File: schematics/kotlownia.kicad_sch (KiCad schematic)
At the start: 5 parts, among them U1 MAX485E, U2 MAX31865xAP

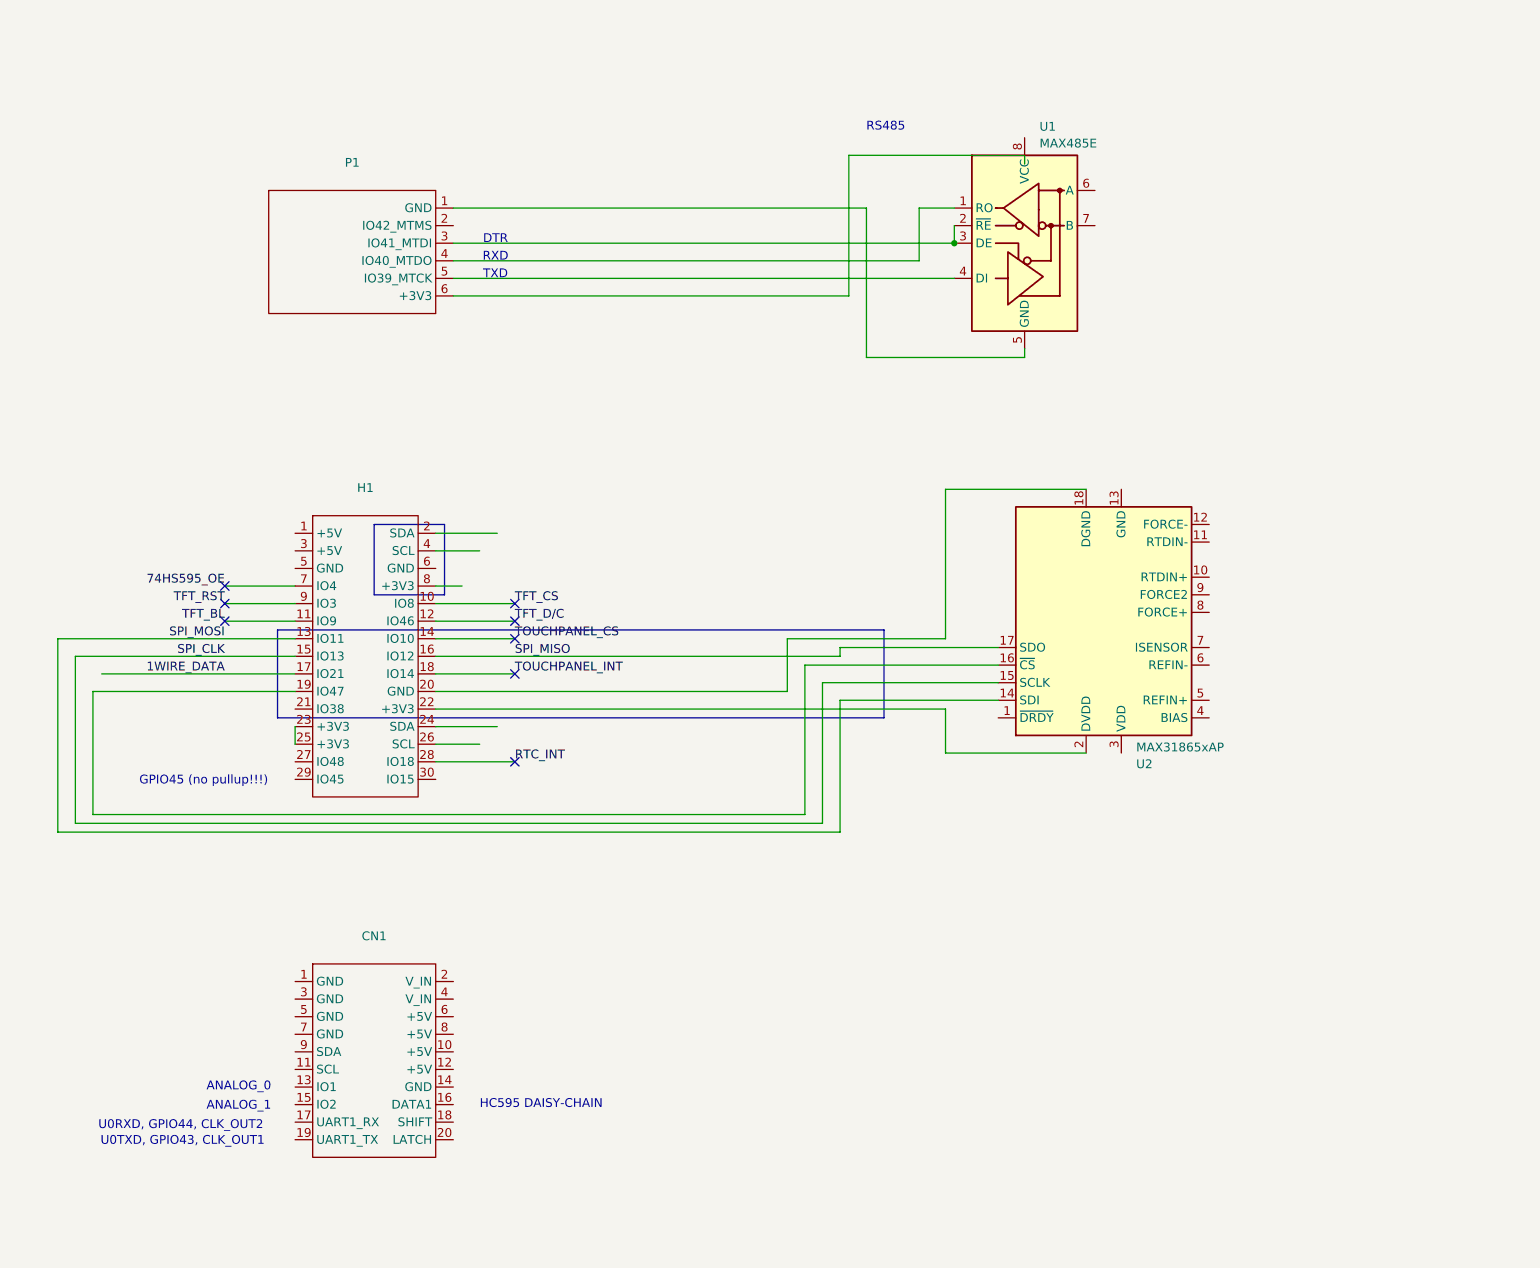
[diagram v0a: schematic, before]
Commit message: chore: hierachical schematics with two MAX31865
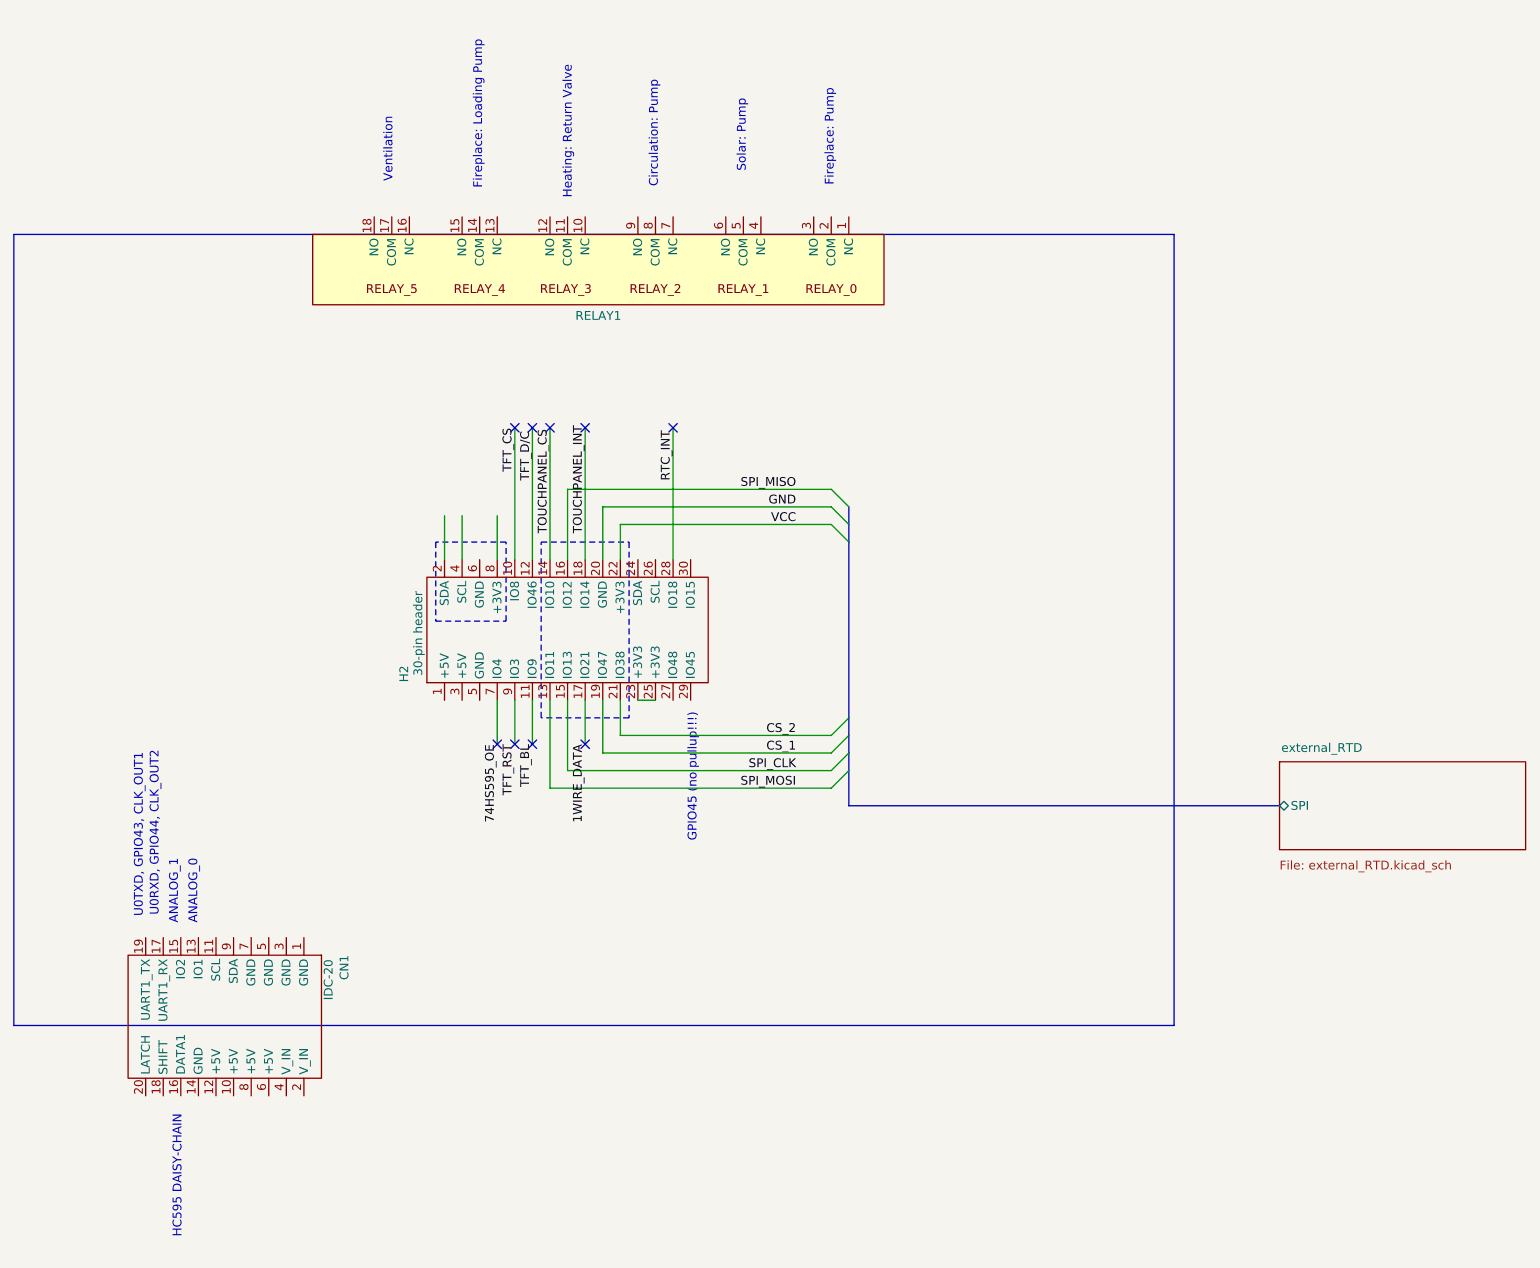
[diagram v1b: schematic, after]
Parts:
- removed H1: ~, symbol T-Relay6:TRelay6-Expansion
- removed P1: ~, symbol T-Relay6:TRelay6-JtagIO
- removed U1: MAX485E, Package_SO:SOIC-8_3.9x4.9mm_P1.27mm, symbol Interface_UART:MAX485E
- removed U2: MAX31865xAP, Package_SO:SSOP-20_5.3x7.2mm_P0.65mm, symbol Sensor_Temperature:MAX31865xAP
- added H2: 30-pin header, symbol T-Relay6:TRelay6-Expansion
- added RELAY1: ~, symbol T-Relay6:T-Relay6-Relays
- CN1: value ~ -> IDC-20
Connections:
- net 1WIRE_DATA: now also H2.17 (IO21)
- net 74HS595_OE: now also H2.7 (IO4)
- net RTC_INT: now also H2.28 (IO18)
- net SPI_CLK: now also H2.15 (IO13)
- net SPI_MISO: now also H2.16 (IO12)
- net SPI_MOSI: now also H2.13 (IO11)
- net TFT_BL: now also H2.11 (IO9)
- net TFT_CS: now also H2.10 (IO8)
- net TFT_D/C: now also H2.12 (IO46)
- net TFT_RST: now also H2.9 (IO3)
- net TOUCHPANEL_CS: now also H2.14 (IO10)
- net TOUCHPANEL_INT: now also H2.18 (IO14)
- new net: H2.23 (+3V3), H2.25 (+3V3)
- new net CS_1: H2.19 (IO47)
- new net CS_2: H2.21 (IO38)
- new net GND: H2.20 (GND)
- new net VCC: H2.22 (+3V3)
- no-connect marks 8 -> 9
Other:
- added sheet external_RTD (external_RTD.kicad_sch)
- note added: "Circulation: Pump"
- note added: "Fireplace: Loading Pump"
- note added: "Fireplace: Pump"
- note added: "Heating: Return Valve"
- note added: "Solar: Pump"
- note added: "Ventilation"
- note removed: "DTR"
- note removed: "RS485"
- note removed: "RXD"
- note removed: "TXD"
- moved on the sheet: CN1

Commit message: chore: more deatils on hierachical schematic
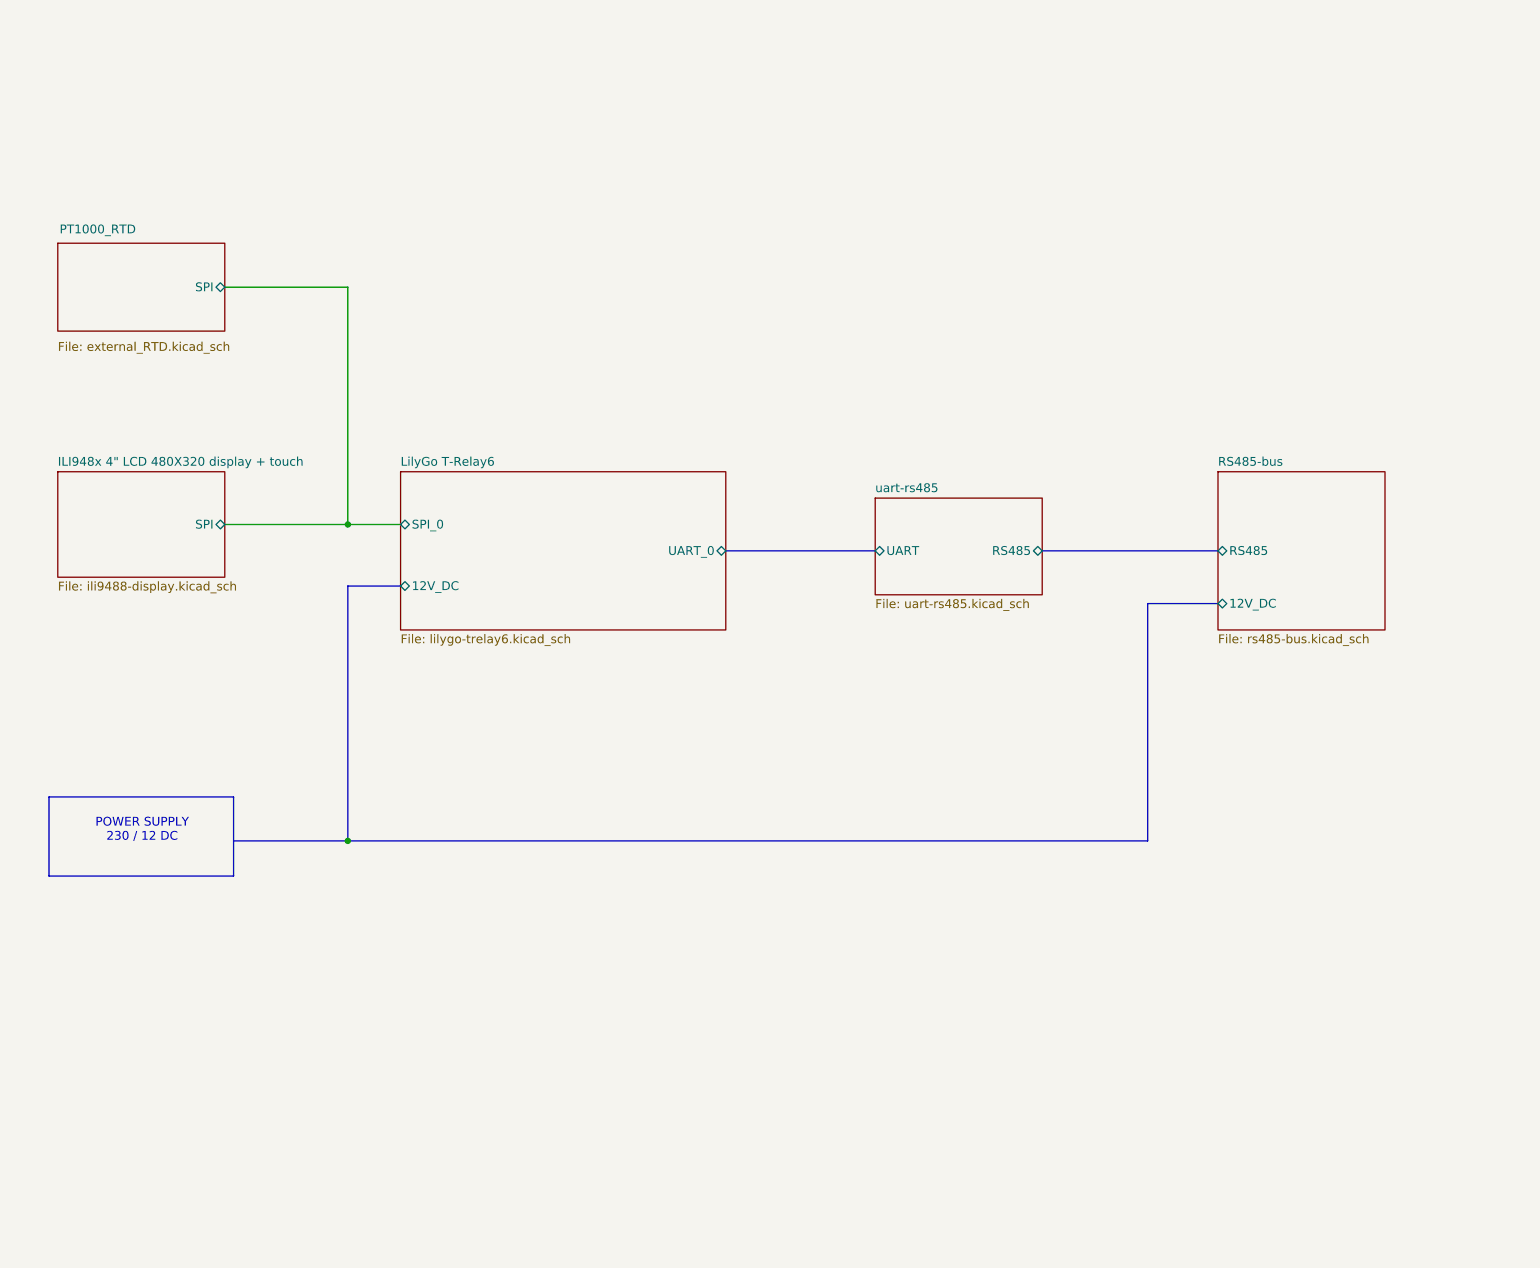
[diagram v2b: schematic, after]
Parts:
- removed CN1: IDC-20, symbol T-Relay6:TRelay6-External
- removed H2: 30-pin header, symbol T-Relay6:TRelay6-Expansion
- removed RELAY1: ~, symbol T-Relay6:T-Relay6-Relays
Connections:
- no-connect marks 9 -> 0
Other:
- sheet external_RTD renamed PT1000_RTD
- added sheet ILI948x 4" LCD 480X320 display + touch (ili9488-display.kicad_sch)
- added sheet LilyGo T-Relay6 (lilygo-trelay6.kicad_sch)
- added sheet RS485-bus (rs485-bus.kicad_sch)
- added sheet uart-rs485 (uart-rs485.kicad_sch)
- note added: "POWER SUPPLY 230 / 12 DC"
- note removed: "ANALOG_0"
- note removed: "ANALOG_1"
- note removed: "Circulation: Pump"
- note removed: "Fireplace: Loading Pump"
- note removed: "Fireplace: Pump"
- note removed: "GPIO45 (no pullup!!!)"
- note removed: "HC595 DAISY-CHAIN"
- note removed: "Heating: Return Valve"
- note removed: "Solar: Pump"
- note removed: "U0RXD, GPIO44, CLK_OUT2"
- note removed: "U0TXD, GPIO43, CLK_OUT1"
- note removed: "Ventilation"
